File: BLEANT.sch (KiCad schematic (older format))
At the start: 50 parts, among them IC1 FAN4010IL6X_F113, IC2 FAN4010IL6X_F113, J1 Conn_01x04_Male, J2 SC_19-20, J3 Conn_01x02, J4 Conn_01x02, U1 nRF51x22-QFxx, U2 LM50BIM3, U3 MP5077GG-Z, U4 MP5077GG-Z, X2 32.768kHz, Y1 16MHz

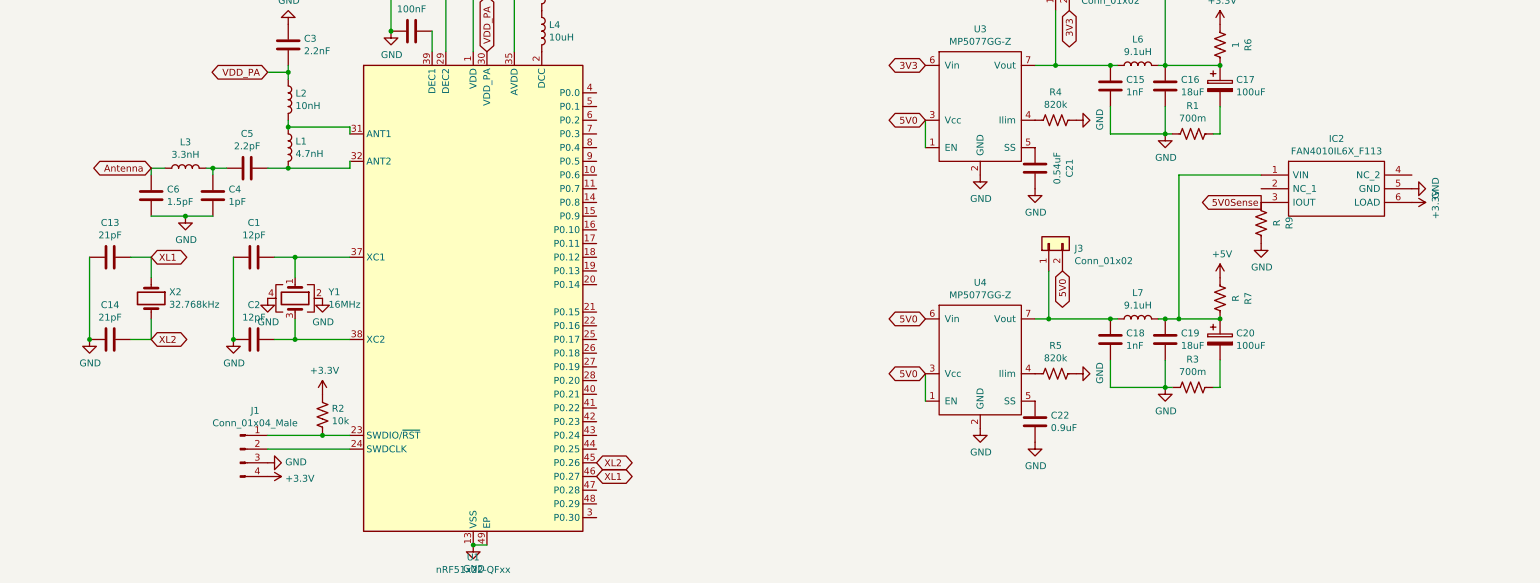
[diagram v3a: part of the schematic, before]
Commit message: added matching network. ruined half the other routing
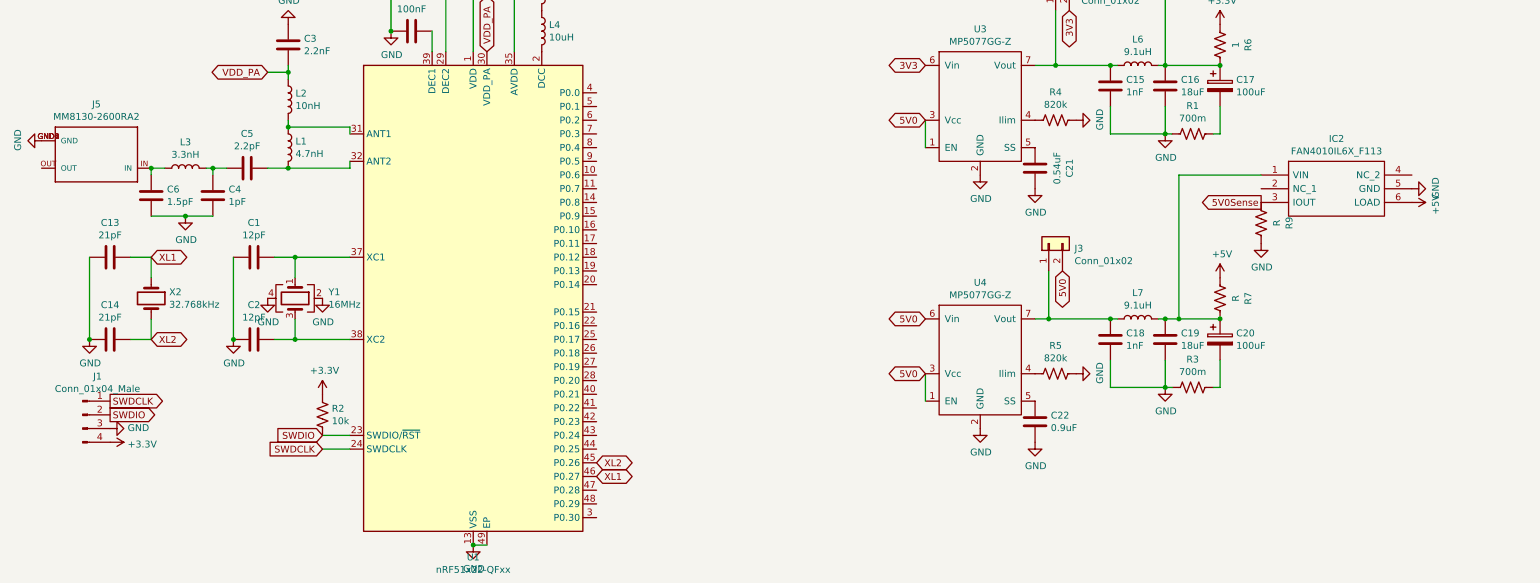
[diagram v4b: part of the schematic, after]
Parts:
- added J5: MM8130-2600RA2, MM8130:MURATA_MM8130-2600RA2, symbol MM8130-2600RA2:MM8130-2600RA2
- C21, C22: footprint (none) -> Capacitor_SMD:C_0805_2012Metric_Pad1.15x1.40mm_HandSolder
- C3, C4, C5, C6: footprint (none) -> Capacitor_SMD:C_0402_1005Metric
- L1, L2, L3: footprint (none) -> Inductor_SMD:L_0402_1005Metric
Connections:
- net +3V3: no longer IC2.6 (LOAD)
- net +5V: now also IC2.6 (LOAD)
- net GND: now also J5.GND1 (GND), J5.GND2 (GND), J5.GND3 (GND), J5.GND4 (GND)
- net SWDIO: now reaches R2.2, U1.23 (SWDIO/~RST)
- net SWDIO: now also J1.2 (Pin_2); no longer J1.1 (Pin_1)
- net SWDCLK: now reaches U1.24 (SWDCLK)
- net SWDCLK: now also J1.1 (Pin_1); no longer J1.2 (Pin_2)
- net Antenna: no longer names the net of C6.1, L3.1
- net Antenna: now also J5.IN
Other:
- moved on the sheet: J1
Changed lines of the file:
@@
 Text GLabel 4000 2750 1    50   BiDi ~ 0
 VDD_PA
-$Comp
-L Device:L L2
-U 1 1 5DF7B422
-P 2550 3100
-F 0 "L2" H 2603 3146 50  0000 L CNN
-F 1 "10nH" H 2603 3055 50  0000 L CNN
-F 2 "" H 2550 3100 50  0001 C CNN
-F 3 "~" H 2550 3100 50  0001 C CNN
-	1    2550 3100
-	1    0    0    -1
-$EndComp
-$Comp
-L Device:L L1
-U 1 1 5DF7C039
-P 2550 3450
-F 0 "L1" H 2603 3496 50  0000 L CNN
-F 1 "4.7nH" H 2603 3405 50  0000 L CNN
-F 2 "" H 2550 3450 50  0001 C CNN
-F 3 "~" H 2550 3450 50  0001 C CNN
-	1    2550 3450
-	1    0    0    -1
-$EndComp
-$Comp
-L Device:C C5
-U 1 1 5DF7CB03
-P 2250 3600
-F 0 "C5" V 1998 3600 50  0000 C CNN
-F 1 "2.2pF" V 2089 3600 50  0000 C CNN
-F 2 "" H 2288 3450 50  0001 C CNN
-F 3 "~" H 2250 3600 50  0001 C CNN
-	1    2250 3600
-	0    1    1    0
-$EndComp
-Wire Wire Line
-	3000 3350 3000 3300
-Wire Wire Line
-	3000 3300 2550 3300
-Wire Wire Line
-	3000 3550 3000 3600
-Wire Wire Line
-	3000 3600 2550 3600
-Wire Wire Line
-	2550 3250 2550 3300
-Connection ~ 2550 3300
-$Comp
-L Device:C C3
-U 1 1 5DF7FAB1
-P 2550 2700
-F 0 "C3" H 2665 2746 50  0000 L CNN
-F 1 "2.2nF" H 2665 2655 50  0000 L CNN
-F 2 "" H 2588 2550 50  0001 C CNN
-F 3 "~" H 2550 2700 50  0001 C CNN
-	1    2550 2700
-	1    0    0    -1
-$EndComp
-$Comp
-L power:GND #PWR0106
-U 1 1 5DF80150
-P 2550 2550
-F 0 "#PWR0106" H 2550 2300 50  0001 C CNN
-F 1 "GND" H 2555 2377 50  0000 C CNN
-F 2 "" H 2550 2550 50  0001 C CNN
-F 3 "" H 2550 2550 50  0001 C CNN
-	1    2550 2550
-	1    0    0    1
-$EndComp
-Text GLabel 2400 2900 0    50   BiDi ~ 0
-VDD_PA
-Wire Wire Line
-	2550 2950 2550 2900
-Wire Wire Line
-	2400 2900 2550 2900
-Connection ~ 2550 2900
-Wire Wire Line
-	2550 2900 2550 2850
-$Comp
-L Device:L L3
-U 1 1 5DF82292
-P 1800 3600
-F 0 "L3" V 1990 3600 50  0000 C CNN
-F 1 "3.3nH" V 1899 3600 50  0000 C CNN
-F 2 "" H 1800 3600 50  0001 C CNN
-F 3 "~" H 1800 3600 50  0001 C CNN
-	1    1800 3600
-	0    -1   -1   0
-$EndComp
-$Comp
-L Device:C C4
-U 1 1 5DF82C3E
-P 2000 3800
-F 0 "C4" H 2115 3846 50  0000 L CNN
-F 1 "1pF" H 2115 3755 50  0000 L CNN
-F 2 "" H 2038 3650 50  0001 C CNN
-F 3 "~" H 2000 3800 50  0001 C CNN
-	1    2000 3800
-	1    0    0    -1
-$EndComp
-$Comp
-L Device:C C6
-U 1 1 5DF837B8
-P 1550 3800
-F 0 "C6" H 1665 3846 50  0000 L CNN
-F 1 "1.5pF" H 1665 3755 50  0000 L CNN
-F 2 "" H 1588 3650 50  0001 C CNN
-F 3 "~" H 1550 3800 50  0001 C CNN
-	1    1550 3800
-	1    0    0    -1
-$EndComp
-Wire Wire Line
-	2400 3600 2550 3600
-Connection ~ 2550 3600
-Wire Wire Line
-	2100 3600 2000 3600
-Wire Wire Line
-	2000 3650 2000 3600
-Connection ~ 2000 3600
-Wire Wire Line
-	2000 3600 1950 3600
-Wire Wire Line
-	1550 3600 1550 3650
-Wire Wire Line
-	2000 3950 1800 3950
-$Comp
-L power:GND #PWR0107
-U 1 1 5DF85D83
-P 1800 3950
-F 0 "#PWR0107" H 1800 3700 50  0001 C CNN
-F 1 "GND" H 1805 3777 50  0000 C CNN
-F 2 "" H 1800 3950 50  0001 C CNN
-F 3 "" H 1800 3950 50  0001 C CNN
-	1    1800 3950
-	1    0    0    -1
-$EndComp
-Text GLabel 1550 3600 0    50   BiDi ~ 0
-Antenna
-Wire Wire Line
-	1550 3950 1800 3950
-Connection ~ 1800 3950
-Wire Wire Line
-	1550 3600 1650 3600
 Wire Wire Line
 	3000 4250 2600 4250
@@
 L Connector:Conn_01x04_Male J1
 U 1 1 5DFB3EF7
-P 2200 5650
-F 0 "J1" H 2308 5931 50  0000 C CNN
-F 1 "Conn_01x04_Male" H 2308 5840 50  0000 C CNN
-F 2 "Connector_PinHeader_2.54mm:PinHeader_1x04_P2.54mm_Vertical" H 2200 5650 50  0001 C CNN
-F 3 "~" H 2200 5650 50  0001 C CNN
-	1    2200 5650
+P 1050 5400
+F 0 "J1" H 1158 5681 50  0000 C CNN
+F 1 "Conn_01x04_Male" H 1158 5590 50  0000 C CNN
+F 2 "Connector_PinHeader_2.54mm:PinHeader_1x04_P2.54mm_Vertical" H 1050 5400 50  0001 C CNN
+F 3 "~" H 1050 5400 50  0001 C CNN
+	1    1050 5400
 	1    0    0    -1
 $EndComp
@@
 L power:GND #PWR0110
 U 1 1 5DFB6ECA
-P 2400 5750
-F 0 "#PWR0110" H 2400 5500 50  0001 C CNN
-F 1 "GND" V 2405 5622 50  0000 R CNN
-F 2 "" H 2400 5750 50  0001 C CNN
-F 3 "" H 2400 5750 50  0001 C CNN
-	1    2400 5750
+P 1250 5500
+F 0 "#PWR0110" H 1250 5250 50  0001 C CNN
+F 1 "GND" V 1255 5372 50  0000 R CNN
+F 2 "" H 1250 5500 50  0001 C CNN
+F 3 "" H 1250 5500 50  0001 C CNN
+	1    1250 5500
 	0    -1   -1   0
 $EndComp
@@
 L power:+3.3V #PWR0111
 U 1 1 5DFB7A76
-P 2400 5850
-F 0 "#PWR0111" H 2400 5700 50  0001 C CNN
-F 1 "+3.3V" V 2415 5978 50  0000 L CNN
-F 2 "" H 2400 5850 50  0001 C CNN
-F 3 "" H 2400 5850 50  0001 C CNN
-	1    2400 5850
+P 1250 5600
+F 0 "#PWR0111" H 1250 5450 50  0001 C CNN
+F 1 "+3.3V" V 1265 5728 50  0000 L CNN
+F 2 "" H 1250 5600 50  0001 C CNN
+F 3 "" H 1250 5600 50  0001 C CNN
+	1    1250 5600
 	0    1    1    0
 $EndComp
@@
 Wire Wire Line
 	2800 5550 3000 5550
-Wire Wire Line
-	2400 5550 2800 5550
-Connection ~ 2800 5550
-Wire Wire Line
-	2400 5650 3000 5650
 Connection ~ 9350 2850
 $Comp
@@
 F 0 "C21" V 7748 3600 50  0000 C CNN
 F 1 "0.54uF" V 7839 3600 50  0000 C CNN
-F 2 "" H 8038 3450 50  0001 C CNN
+F 2 "Capacitor_SMD:C_0805_2012Metric_Pad1.15x1.40mm_HandSolder" H 8038 3450 50  0001 C CNN
 F 3 "~" H 8000 3600 50  0001 C CNN
 	1    8000 3600
@@
 F 0 "C22" H 7885 5404 50  0000 R CNN
 F 1 "0.9uF" H 7885 5495 50  0000 R CNN
-F 2 "" H 8038 5300 50  0001 C CNN
+F 2 "Capacitor_SMD:C_0805_2012Metric_Pad1.15x1.40mm_HandSolder" H 8038 5300 50  0001 C CNN
 F 3 "~" H 8000 5450 50  0001 C CNN
 	1    8000 5450
@@
 $EndComp
 $Comp
-L power:+3.3V #PWR0133
-U 1 1 5E07C9C1
-P 10750 3850
-F 0 "#PWR0133" H 10750 3700 50  0001 C CNN
-F 1 "+3.3V" H 10765 4023 50  0000 C CNN
-F 2 "" H 10750 3850 50  0001 C CNN
-F 3 "" H 10750 3850 50  0001 C CNN
-	1    10750 3850
-	0    1    1    0
-$EndComp
-$Comp
 L FAN4010IL6X_F113:FAN4010IL6X_F113 IC2
 U 1 1 5E07C9D3
@@
 	1    0    0    -1
 $EndComp
+Text GLabel 2800 5550 0    50   Input ~ 0
+SWDIO
+Text GLabel 2800 5650 0    50   Input ~ 0
+SWDCLK
+Wire Wire Line
+	3000 5650 2800 5650
+Text GLabel 1250 5400 2    50   Output ~ 0
+SWDIO
+Text GLabel 1250 5300 2    50   Output ~ 0
+SWDCLK
+Wire Wire Line
+	3000 3350 3000 3300
+Text GLabel 2400 2900 0    50   BiDi ~ 0
+VDD_PA
+$Comp
+L power:GND #PWR06
+U 1 1 5E09E24E
+P 750 3400
+F 0 "#PWR06" H 750 3150 50  0001 C CNN
+F 1 "GND" H 755 3227 50  0000 C CNN
+F 2 "" H 750 3400 50  0001 C CNN
+F 3 "" H 750 3400 50  0001 C CNN
+	1    750  3400
+	0    1    -1   0
+$EndComp
+$Comp
+L MM8130-2600RA2:MM8130-2600RA2 J5
+U 1 1 5E09C26A
+P 1150 3500
+F 0 "J5" H 1150 3133 50  0000 C CNN
+F 1 "MM8130-2600RA2" H 1150 3224 50  0000 C CNN
+F 2 "MM8130:MURATA_MM8130-2600RA2" H 1150 3500 50  0001 L BNN
+F 3 "MURATA" H 1150 3500 50  0001 L BNN
+	1    1150 3500
+	-1   0    0    1
+$EndComp
+Wire Wire Line
+	1550 3600 1550 3650
+Connection ~ 1550 3600
+Wire Wire Line
+	1550 3600 1650 3600
+$Comp
+L Device:C C6
+U 1 1 5DF837B8
+P 1550 3800
+F 0 "C6" H 1665 3846 50  0000 L CNN
+F 1 "1.5pF" H 1665 3755 50  0000 L CNN
+F 2 "Capacitor_SMD:C_0402_1005Metric" H 1588 3650 50  0001 C CNN
+F 3 "~" H 1550 3800 50  0001 C CNN
+	1    1550 3800
+	1    0    0    -1
+$EndComp
+Wire Wire Line
+	1550 3950 1800 3950
+$Comp
+L power:GND #PWR0107
+U 1 1 5DF85D83
+P 1800 3950
+F 0 "#PWR0107" H 1800 3700 50  0001 C CNN
+F 1 "GND" H 1805 3777 50  0000 C CNN
+F 2 "" H 1800 3950 50  0001 C CNN
+F 3 "" H 1800 3950 50  0001 C CNN
+	1    1800 3950
+	1    0    0    -1
+$EndComp
+Connection ~ 1800 3950
+Wire Wire Line
+	2000 3950 1800 3950
+Wire Wire Line
+	2000 3650 2000 3600
+Wire Wire Line
+	2000 3600 1950 3600
+$Comp
+L Device:C C4
+U 1 1 5DF82C3E
+P 2000 3800
+F 0 "C4" H 2115 3846 50  0000 L CNN
+F 1 "1pF" H 2115 3755 50  0000 L CNN
+F 2 "Capacitor_SMD:C_0402_1005Metric" H 2038 3650 50  0001 C CNN
+F 3 "~" H 2000 3800 50  0001 C CNN
+	1    2000 3800
+	1    0    0    -1
+$EndComp
+$Comp
+L Device:L L3
+U 1 1 5DF82292
+P 1800 3600
+F 0 "L3" V 1990 3600 50  0000 C CNN
+F 1 "3.3nH" V 1899 3600 50  0000 C CNN
+F 2 "Inductor_SMD:L_0402_1005Metric" H 1800 3600 50  0001 C CNN
+F 3 "~" H 1800 3600 50  0001 C CNN
+	1    1800 3600
+	0    -1   -1   0
+$EndComp
+Connection ~ 2000 3600
+Wire Wire Line
+	2100 3600 2000 3600
+$Comp
+L Device:C C5
+U 1 1 5DF7CB03
+P 2250 3600
+F 0 "C5" V 1998 3600 50  0000 C CNN
+F 1 "2.2pF" V 2089 3600 50  0000 C CNN
+F 2 "Capacitor_SMD:C_0402_1005Metric" H 2288 3450 50  0001 C CNN
+F 3 "~" H 2250 3600 50  0001 C CNN
+	1    2250 3600
+	0    1    1    0
+$EndComp
+Wire Wire Line
+	3000 3550 3000 3600
+Wire Wire Line
+	2400 3600 2550 3600
+Wire Wire Line
+	3000 3600 2550 3600
+Connection ~ 2550 3600
+$Comp
+L Device:L L1
+U 1 1 5DF7C039
+P 2550 3450
+F 0 "L1" H 2603 3496 50  0000 L CNN
+F 1 "4.7nH" H 2603 3405 50  0000 L CNN
+F 2 "Inductor_SMD:L_0402_1005Metric" H 2550 3450 50  0001 C CNN
+F 3 "~" H 2550 3450 50  0001 C CNN
+	1    2550 3450
+	1    0    0    -1
+$EndComp
+Wire Wire Line
+	3000 3300 2550 3300
+Connection ~ 2550 3300
+Wire Wire Line
+	2550 3250 2550 3300
+$Comp
+L Device:L L2
+U 1 1 5DF7B422
+P 2550 3100
+F 0 "L2" H 2603 3146 50  0000 L CNN
+F 1 "10nH" H 2603 3055 50  0000 L CNN
+F 2 "Inductor_SMD:L_0402_1005Metric" H 2550 3100 50  0001 C CNN
+F 3 "~" H 2550 3100 50  0001 C CNN
+	1    2550 3100
+	1    0    0    -1
+$EndComp
+Wire Wire Line
+	2400 2900 2550 2900
+Wire Wire Line
+	2550 2900 2550 2850
+Connection ~ 2550 2900
+Wire Wire Line
+	2550 2950 2550 2900
+$Comp
+L Device:C C3
+U 1 1 5DF7FAB1
+P 2550 2700
+F 0 "C3" H 2665 2746 50  0000 L CNN
+F 1 "2.2nF" H 2665 2655 50  0000 L CNN
+F 2 "Capacitor_SMD:C_0402_1005Metric" H 2588 2550 50  0001 C CNN
+F 3 "~" H 2550 2700 50  0001 C CNN
+	1    2550 2700
+	1    0    0    -1
+$EndComp
+$Comp
+L power:GND #PWR0106
+U 1 1 5DF80150
+P 2550 2550
+F 0 "#PWR0106" H 2550 2300 50  0001 C CNN
+F 1 "GND" H 2555 2377 50  0000 C CNN
+F 2 "" H 2550 2550 50  0001 C CNN
+F 3 "" H 2550 2550 50  0001 C CNN
+	1    2550 2550
+	1    0    0    1
+$EndComp
+$Comp
+L power:+5V #PWR0133
+U 1 1 5E0D52E2
+P 10750 3850
+F 0 "#PWR0133" H 10750 3700 50  0001 C CNN
+F 1 "+5V" H 10765 4023 50  0000 C CNN
+F 2 "" H 10750 3850 50  0001 C CNN
+F 3 "" H 10750 3850 50  0001 C CNN
+	1    10750 3850
+	0    1    1    0
+$EndComp
 $EndSCHEMATC

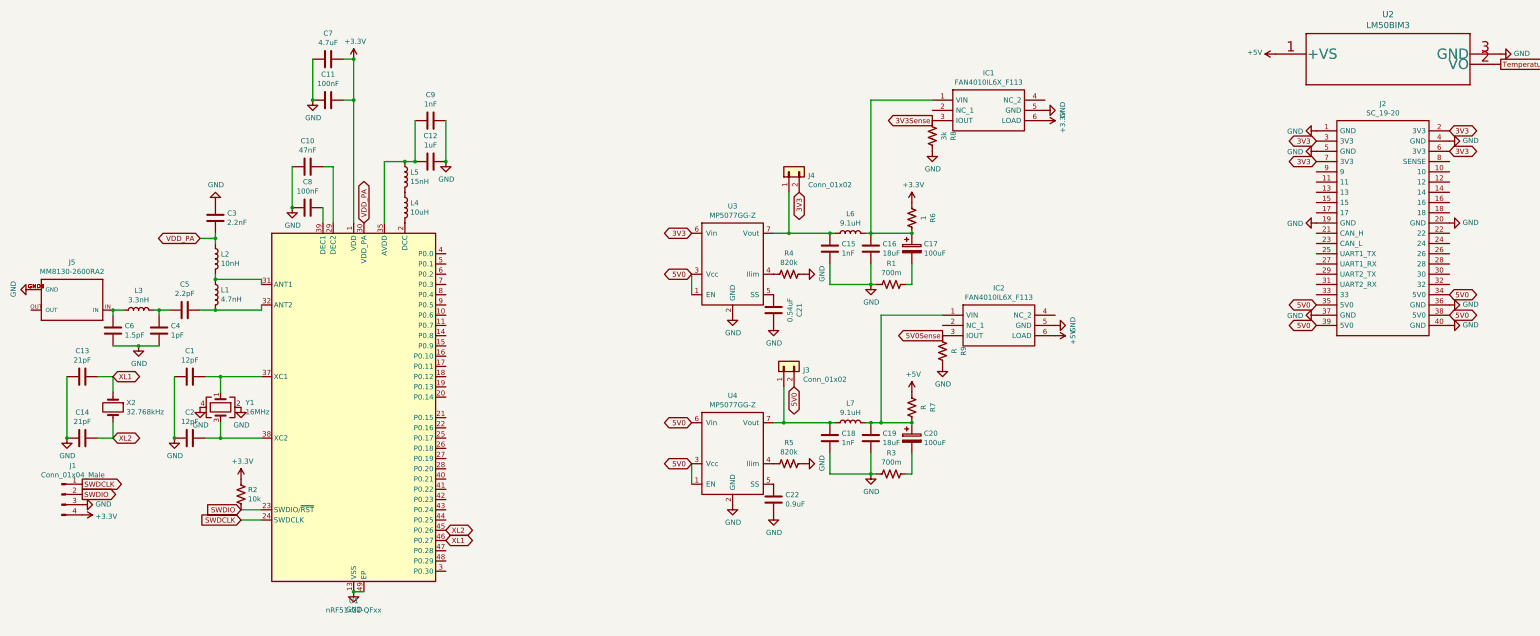
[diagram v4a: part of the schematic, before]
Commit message: Placed all components. Need to add GPIO connections
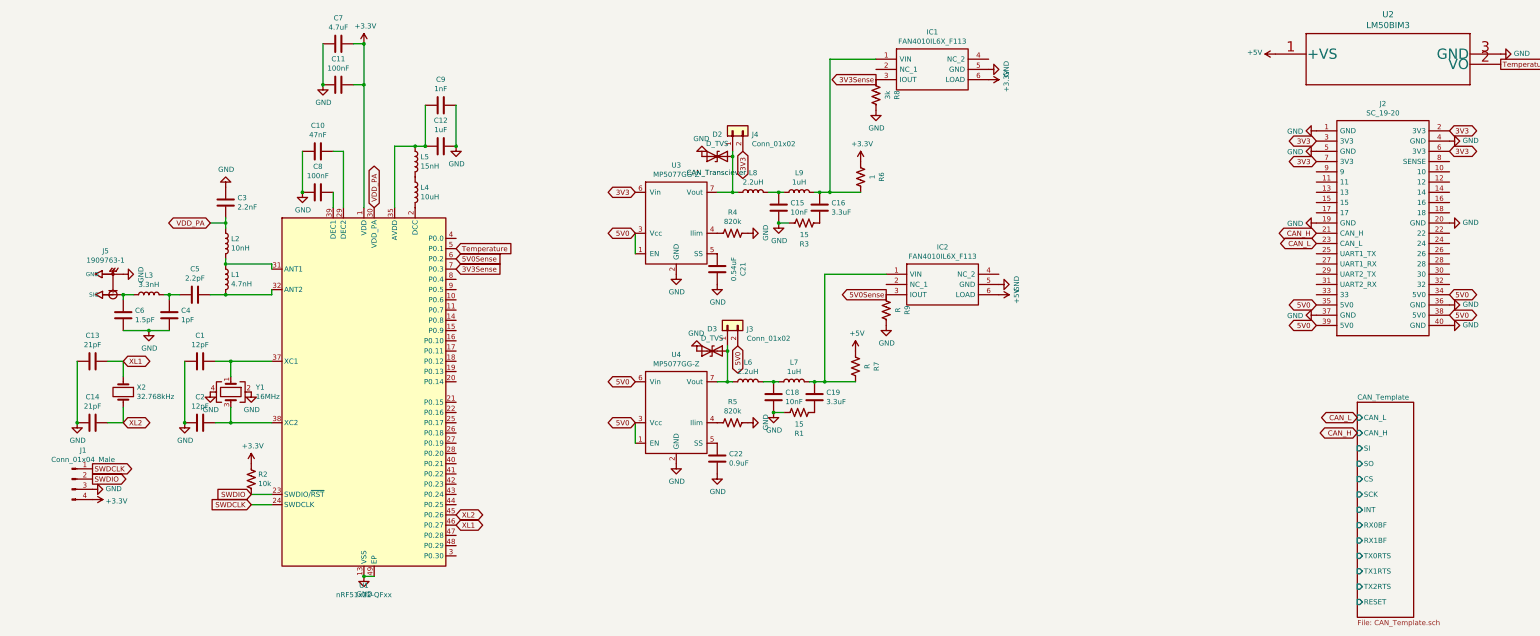
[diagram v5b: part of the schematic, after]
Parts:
- removed C17, C20: 100uF, symbol Device:CP
- removed J5: MM8130-2600RA2, MM8130:MURATA_MM8130-2600RA2, symbol MM8130-2600RA2:MM8130-2600RA2
- added D2, D3: D_TVS, Diode_SMD:D_SOD-523, symbol Device:D_TVS
- added J5: 1909763-1, U:TE_1909763-1, symbol 1909763-1:1909763-1
- added L8: 2.2uH, Inductor_SMD:L_0402_1005Metric, symbol Device:L
- added L9: 1uH, Inductor_SMD:L_0402_1005Metric, symbol Device:L
- C1, C10, C11, C12, C13, C14, C2, C21, C22, C7, C8, C9: footprint Capacitor_SMD:C_0805_2012Metric_Pad1.15x1.40mm_HandSolder -> Capacitor_SMD:C_0402_1005Metric
- C15, C18: value 1nF -> 10nF; footprint Capacitor_SMD:C_0805_2012Metric_Pad1.15x1.40mm_HandSolder -> Capacitor_SMD:C_0402_1005Metric
- C16, C19: value 18uF -> 3.3uF; footprint Capacitor_SMD:C_0805_2012Metric_Pad1.15x1.40mm_HandSolder -> Capacitor_SMD:C_0402_1005Metric
- L4, L5: footprint Inductor_SMD:L_0805_2012Metric_Pad1.15x1.40mm_HandSolder -> Inductor_SMD:L_0402_1005Metric
- L6: value 9.1uH -> 2.2uH; footprint Inductor_SMD:L_0805_2012Metric_Pad1.15x1.40mm_HandSolder -> Inductor_SMD:L_0402_1005Metric
- L7: value 9.1uH -> 1uH; footprint Inductor_SMD:L_0805_2012Metric_Pad1.15x1.40mm_HandSolder -> Inductor_SMD:L_0402_1005Metric
- R1, R3: value 700m -> 15; footprint Resistor_SMD:R_0805_2012Metric_Pad1.15x1.40mm_HandSolder -> Resistor_SMD:R_0402_1005Metric
- R2, R4, R5, R6, R7, R8, R9: footprint Resistor_SMD:R_0805_2012Metric_Pad1.15x1.40mm_HandSolder -> Resistor_SMD:R_0402_1005Metric
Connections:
- net 3V3Sense: now also U1.7 (P0.3)
- net 5V0Sense: now also U1.6 (P0.2)
- net GND: now also R1.2, R3.2, D2.2 (A2), D3.2 (A2), J5.2 (GND), J5.3 (GND); no longer C16.2, C19.2, R1.1, R3.1
- net Temperature: now also U1.5 (P0.1)
- net at C6.1, L3.1: now also J5.1 (SIG)
- net at C16.1, IC1.1 (VIN), R6.2: now also L9.2; no longer L6.2
- net at J4.1 (Pin_1), U3.10 (Vout), U3.7 (Vout)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: now also D2.1 (A1), L8.1; no longer C15.1, L6.1
- net CAN_H: now reaches J2.21 (CAN_H)
- net CAN_L: now reaches J2.23 (CAN_L)
- net at J3.1 (Pin_1), U4.10 (Vout), U4.7 (Vout)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: now also L6.1, D3.1 (A1); no longer C18.1, L7.1
- new net: C19.2, R1.1
- new net: C18.1, L6.2, L7.1
- new net: C16.2, R3.1
- new net: C15.1, L8.2, L9.1
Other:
- moved on the sheet: C1, C10, C11, C12, C13, C14, C18, C19, C2, C21, C22, C3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
